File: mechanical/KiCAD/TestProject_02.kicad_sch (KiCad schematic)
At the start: 29 parts, among them J1 USB_C_Receptacle_USB2.0_16P, J2 C-OBD-II-16M, U1 ESP32-C3-WROOM-02, U2 TPS54302, U3 USBLC6-2P6, U4 SN65HVD231

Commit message: Editing the schematic drawing for the OBD PCB, still needs somepolishing and cleaning up.
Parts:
- added D4: SMAJ24A, Diode_SMD:D_SMA, symbol Diode:SMAJ24A
- added D5: LED_G, LED_SMD:LED_0805_2012Metric, symbol Device:LED
- added D6: LED_B, LED_SMD:LED_0805_2012Metric, symbol Device:LED
- added D7: LED_R, LED_SMD:LED_0805_2012Metric, symbol Device:LED
- added D8: SS34, Diode_SMD:D_SMA, symbol Diode:SS34
- added D9: NUP2105L, Package_TO_SOT_SMD:SOT-23, symbol Power_Protection:NUP2105L
- added R11, R12, R13: 330R, Resistor_SMD:R_0603_1608Metric, symbol Device:R
- added R9: 120R, Resistor_SMD:R_0603_1608Metric, symbol Device:R
- D3: value LED -> LED_G
- renumbered RST1 to BTN1
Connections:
- net +3.3V: now also R8.2, U4.3 (VCC), D8.1 (K)
- net GND: now also J2.4, J2.5, U4.2 (GND), D4.2 (A2), D5.1 (K), D6.1 (K), D7.1 (K), D9.3 (A)
- net USB_D+: now also U1.14 (IO19)
- net USB_D-: now also U1.13 (IO18)
- net CAN_TX: now reaches U4.1 (D)
- net CAN_TX: now also U1.4 (IO5)
- net CAN_RX: now reaches U4.4 (R)
- net CAN_RX: now also U1.3 (IO4)
- net CANL: now reaches U4.6 (CANL)
- net CANL: now also J2.14, D9.2 (K), R9.1
- net CANH: now reaches U4.7 (CANH)
- net CANH: now also J2.6, D9.1 (K), R9.2
- net OPMODE: now reaches U4.8 (Rs)
- net OPMODE: now also U1.10 (IO10)
- net at U1.15 (IO3): now also R12.1
- net at U1.17 (IO1): now also R11.1
- net at U1.7 (IO8): now also R13.1
- net at J2.16: now also D4.1 (A1), D8.2 (A)
- new net: D7.2 (A), R13.2
- new net: D5.2 (A), R11.2
- new net: D6.2 (A), R12.2
- no-connect marks 3 -> 15
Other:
- note added: "Connection Indicator LED"
- note added: "Error Indicator LED"
- note added: "Operation mode selector (High speed, standby, low power) Logic is needed for this from the ESP"
- note added: "Over Voltage Protection Diode"
- note added: "Power Indicator LED"
- note added: "TVS Diode ESD, EFT protection"
- moved on the sheet: BTN1, C2, EN1, J2, R1, R7, U4

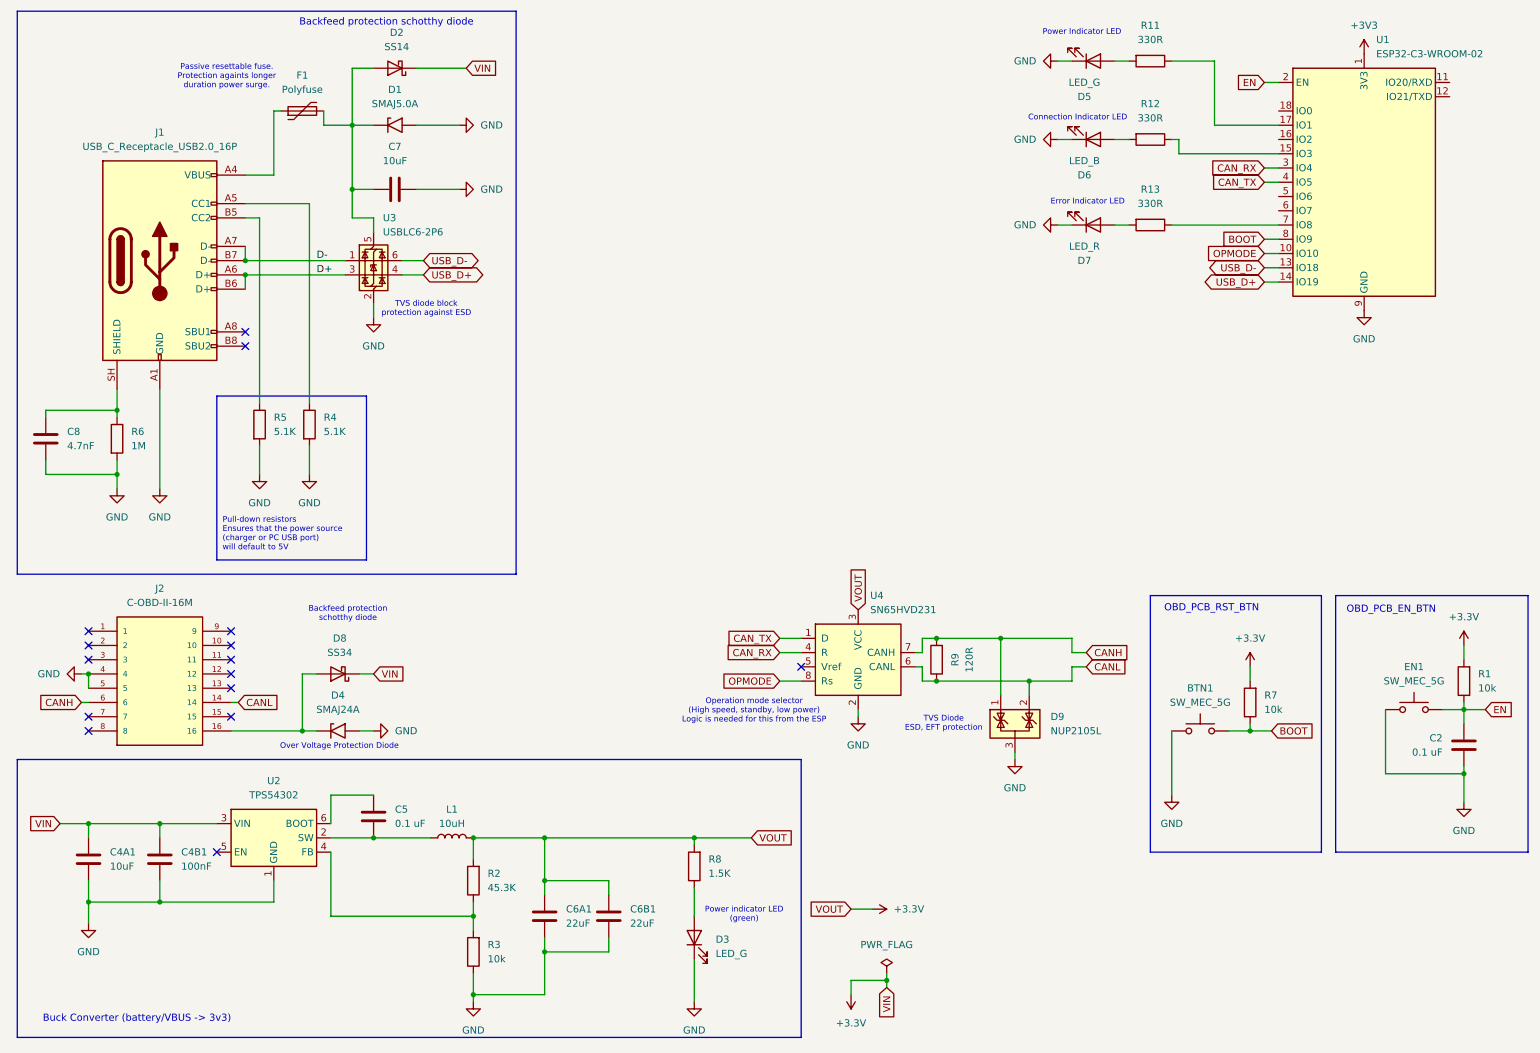
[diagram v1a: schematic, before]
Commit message: Small changes in the schematic layout, organized the components into blocks, changed some wrong footprints
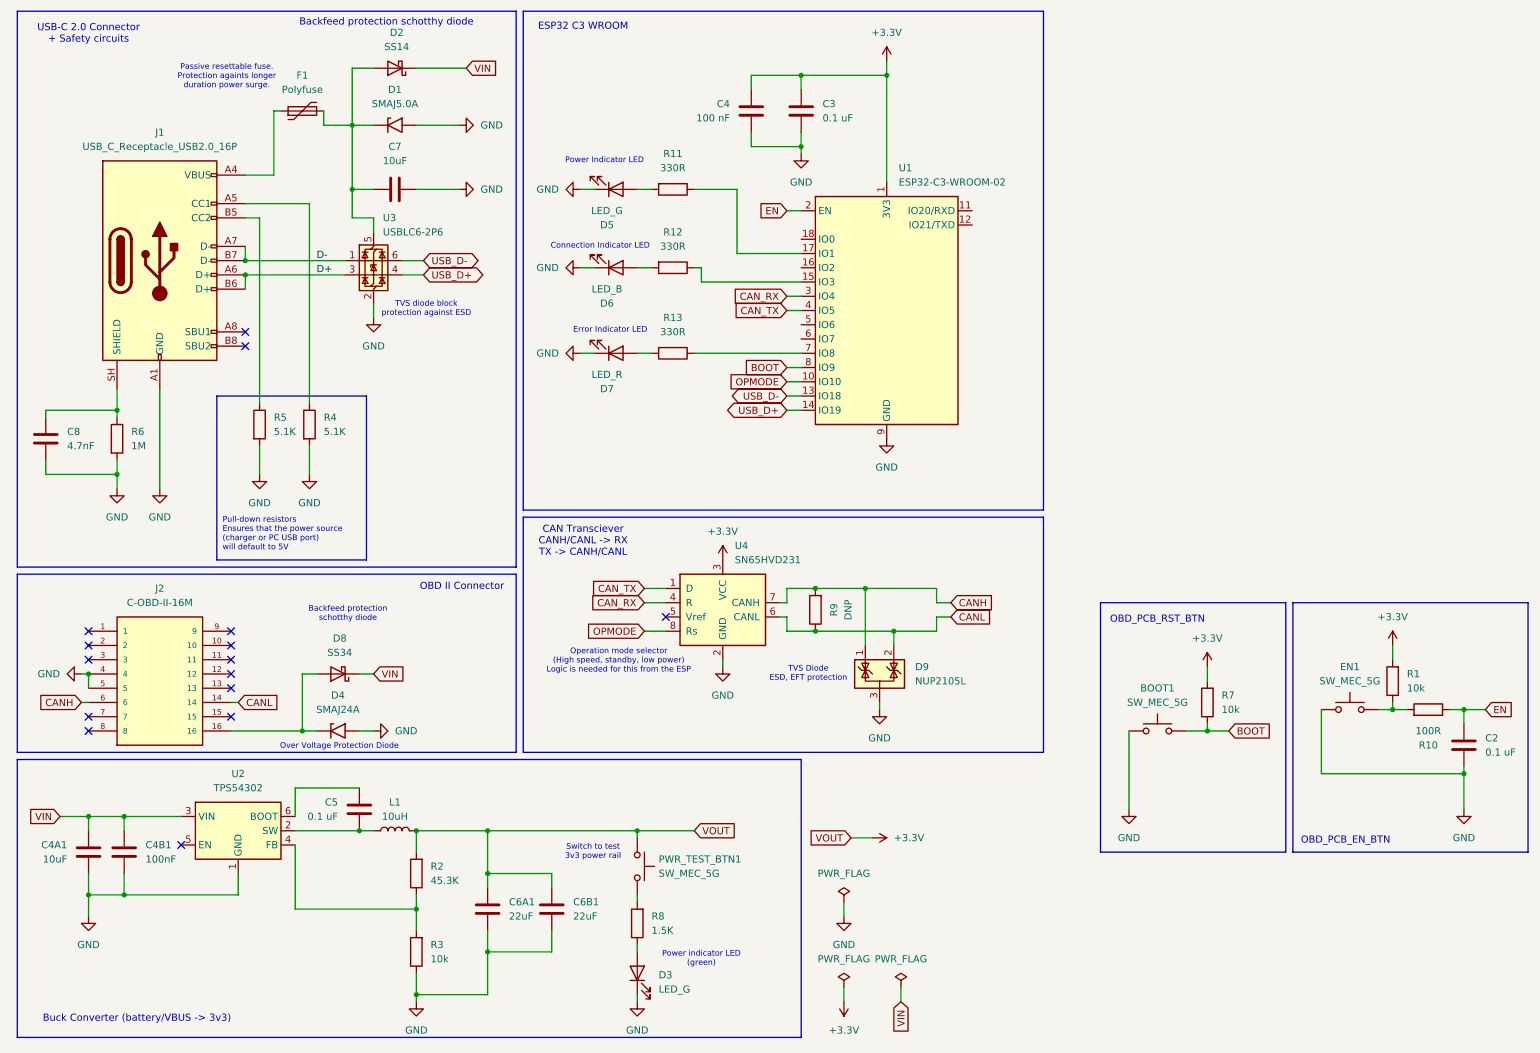
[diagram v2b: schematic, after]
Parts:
- added C3: 0.1 uF, Capacitor_SMD:C_0805_2012Metric, symbol Device:C
- added C4: 100 nF, Capacitor_SMD:C_0805_2012Metric, symbol Device:C
- added PWR_TEST_BTN1: SW_MEC_5G, Button_Switch_SMD:SW_Push_SPST_NO_Alps_SKRK, symbol Switch:SW_MEC_5G
- added R10: 100R, Resistor_SMD:R_0805_2012Metric, symbol Device:R
- BOOT1: renamed from BTN1; footprint Button_Switch_THT:SW_PUSH_1P1T_6x3.5mm_H5.0_APEM_MJTP1250 -> Button_Switch_SMD:SW_Push_SPST_NO_Alps_SKRK
- EN1: footprint Button_Switch_THT:SW_PUSH_1P1T_6x3.5mm_H5.0_APEM_MJTP1250 -> Button_Switch_SMD:SW_Push_SPST_NO_Alps_SKRK
- F1: footprint Fuse:Fuse_Bourns_MF-RHT050 -> Fuse:Fuse_0805_2012Metric
- R11, R12, R13: footprint Resistor_SMD:R_0603_1608Metric -> Resistor_SMD:R_0805_2012Metric
- R9: value 120R -> DNP; footprint Resistor_SMD:R_0603_1608Metric -> Resistor_SMD:R_0805_2012Metric
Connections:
- net +3V3 is gone; now on net +3.3V: U1.1 (3V3)
- net +3.3V: now also C3.1, C4.1, PWR_TEST_BTN1.1 (A), PWR_TEST_BTN1.2 (A); no longer C4A1.1, C4B1.1, D2.1 (K), D8.1 (K), R8.2, U2.3 (VIN)
- net EN: now also R10.1; no longer EN1.3 (B), EN1.4 (B), R1.1
- net GND: now also C3.2, C4.2
- new net: EN1.3 (B), EN1.4 (B), R1.1, R10.2
- new net: PWR_TEST_BTN1.3 (B), PWR_TEST_BTN1.4 (B), R8.2
- new net VIN: C4A1.1, C4B1.1, D2.1 (K), D8.1 (K), U2.3 (VIN)
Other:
- note added: "CAN Transciever CANH/CANL -> RX TX -> CANH/CANL"
- note added: "ESP32 C3 WROOM"
- note added: "OBD II Connector"
- note added: "Switch to test 3v3 power rail"
- note added: "USB-C 2.0 Connector + Safety circuits"
- moved on the sheet: BOOT1, C4A1, C4B1, C5, C6A1, C6B1, D3, D5, D6, D7, D9, EN1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

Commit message: Getting close to finishing the OBD PCB. Still needs some final touch ups, also some safety and reliability check.
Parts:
- removed BOOT1, EN1, PWR_TEST_BTN1: SW_MEC_5G, Button_Switch_SMD:SW_Push_SPST_NO_Alps_SKRK, symbol Switch:SW_MEC_5G
- removed R9: DNP, Resistor_SMD:R_0805_2012Metric, symbol Device:R
- added BOOT2, EN1, TEST_BTN1: SW_MEC_5E, Button_Switch_SMD:SW_SPST_EVQP2_MiddlePushTravel_H2.5mm, symbol Switch:SW_MEC_5E
- added JP1: SolderJumper_2_Open, Jumper:SolderJumper-2_P1.3mm_Open_Pad1.0x1.5mm, symbol Jumper:SolderJumper_2_Open
- C4A1: footprint Capacitor_SMD:C_1206_3216Metric -> Capacitor_SMD:C_0805_2012Metric
- J2: footprint custom_library:COMTECH_C-OBD-II-16M -> C-OBD-II-16M:COMTECH_C-OBD-II-16M
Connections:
- net +3.3V: now also TEST_BTN1.1
- net BOOT: now also BOOT2.1
- net CANH: now also JP1.2 (B)
- net CANL: now also JP1.1 (A)
- net CAN_RX: now also U1.4 (IO5); no longer U1.3 (IO4)
- net CAN_TX: now also U1.3 (IO4); no longer U1.4 (IO5)
- net GND: now also BOOT2.2, EN1.2
- net at R11.1: now also U1.5 (IO6); no longer U1.17 (IO1)
- net at R1.1, R10.2: now also EN1.1
- net at U1.15 (IO3): no longer R12.1
- net at U1.6 (IO7): now also R12.1
- net at R8.2: now also TEST_BTN1.2
- new net: TEST_BTN1.3 (K), TEST_BTN1.4 (A)
- new net: BOOT2.3 (K), BOOT2.4 (A)
- new net: EN1.3 (K), EN1.4 (A)
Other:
- moved on the sheet: D3, D5, D6, D7, R11, R12, R13, R8

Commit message: Relocated buck converter and CAN transciever, added a mounting hole to secure the casing later.
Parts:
- added J3: TXD_PAD, TestPoint:TestPoint_Pad_2.0x2.0mm, symbol Connector:Conn_01x01_Pin
- added J4: RXD_PAD, TestPoint:TestPoint_Pad_2.0x2.0mm, symbol Connector:Conn_01x01_Pin
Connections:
- net at U1.11 (IO20/RXD): now also J3.1 (Pin_1)
- net at U1.12 (IO21/TXD): now also J4.1 (Pin_1)
- no-connect marks 15 -> 19
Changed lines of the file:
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@@
 	(rectangle
 		(start 104.14 13.97)
-		(end 196.85 102.87)
+		(end 210.82 102.87)
 		(stroke
 			(width 0)
@@
 	)
 	(junction
-		(at 170.18 125.73)
-		(diameter 0)
-		(color 0 0 0 0)
-	)
-	(junction
 		(at 97.79 160.02)
 		(diameter 0)
@@
 	)
 	(junction
+		(at 170.18 125.73)
+		(diameter 0)
+		(color 0 0 0 0)
+	)
+	(junction
 		(at 54.61 58.42)
 		(diameter 0)
@@
 	)
 	(no_connect
+		(at 153.67 59.69)
+	)
+	(no_connect
 		(at 54.61 71.12)
 	)
 	(no_connect
+		(at 153.67 62.23)
+	)
+	(no_connect
 		(at 52.07 134.62)
 	)
@@
 	)
 	(no_connect
+		(at 153.67 57.15)
+	)
+	(no_connect
+		(at 153.67 54.61)
+	)
+	(no_connect
 		(at 26.67 142.24)
 	)
@@
 	(wire
 		(pts
+			(xy 165.1 115.57) (xy 177.8 115.57)
+		)
+		(stroke
+			(width 0)
+			(type default)
+		)
+	)
+	(wire
+		(pts
 			(xy 177.8 121.92) (xy 177.8 125.73)
 		)
@@
 	(wire
 		(pts
+			(xy 186.69 54.61) (xy 186.69 52.07)
+		)
+		(stroke
+			(width 0)
+			(type default)
+		)
+	)
+	(wire
+		(pts
 			(xy 26.67 171.45) (xy 26.67 175.26)
 		)
@@
 	(wire
 		(pts
+			(xy 170.18 125.73) (xy 170.18 127)
+		)
+		(stroke
+			(width 0)
+			(type default)
+		)
+	)
+	(wire
+		(pts
 			(xy 97.79 167.64) (xy 97.79 160.02)
 		)
@@
 	(wire
 		(pts
+			(xy 186.69 52.07) (xy 184.15 52.07)
+		)
+		(stroke
+			(width 0)
+			(type default)
+		)
+	)
+	(wire
+		(pts
 			(xy 73.66 34.29) (xy 77.47 34.29)
 		)
@@
 	(wire
 		(pts
-			(xy 68.58 34.29) (xy 73.66 34.29)
+			(xy 170.18 125.73) (xy 177.8 125.73)
 		)
 		(stroke
@@
 	(wire
 		(pts
-			(xy 39.37 81.28) (xy 39.37 99.06)
+			(xy 68.58 34.29) (xy 73.66 34.29)
 		)
 		(stroke
@@
 	(wire
 		(pts
-			(xy 64.77 132.08) (xy 67.31 132.08)
+			(xy 39.37 81.28) (xy 39.37 99.06)
 		)
 		(stroke
@@
 	(wire
 		(pts
-			(xy 177.8 119.38) (xy 177.8 115.57)
+			(xy 64.77 132.08) (xy 67.31 132.08)
 		)
 		(stroke
@@
 	(wire
 		(pts
-			(xy 170.18 125.73) (xy 177.8 125.73)
+			(xy 177.8 119.38) (xy 177.8 115.57)
 		)
 		(stroke
@@
 	(wire
 		(pts
-			(xy 165.1 115.57) (xy 177.8 115.57)
-		)
-		(stroke
-			(width 0)
-			(type default)
-		)
-	)
-	(wire
-		(pts
 			(xy 151.13 77.47) (xy 153.67 77.47)
 		)
@@
 	(wire
 		(pts
+			(xy 165.1 115.57) (xy 165.1 127)
+		)
+		(stroke
+			(width 0)
+			(type default)
+		)
+	)
+	(wire
+		(pts
 			(xy 151.13 121.92) (xy 151.13 125.73)
 		)
@@
 	(wire
 		(pts
-			(xy 168.91 22.86) (xy 168.91 25.4)
+			(xy 184.15 49.53) (xy 189.23 49.53)
 		)
 		(stroke
@@
 	(wire
 		(pts
-			(xy 161.29 187.96) (xy 161.29 190.5)
+			(xy 168.91 22.86) (xy 168.91 25.4)
 		)
 		(stroke
@@
 	(wire
 		(pts
-			(xy 165.1 115.57) (xy 165.1 127)
+			(xy 161.29 187.96) (xy 161.29 190.5)
 		)
 		(stroke
@@
 	(wire
 		(pts
+			(xy 189.23 49.53) (xy 189.23 62.23)
+		)
+		(stroke
+			(width 0)
+			(type default)
+		)
+	)
+	(wire
+		(pts
 			(xy 256.54 138.43) (xy 259.08 138.43)
 		)
@@
 	(wire
 		(pts
-			(xy 170.18 125.73) (xy 170.18 127)
-		)
-		(stroke
-			(width 0)
-			(type default)
-		)
-	)
-	(wire
-		(pts
 			(xy 135.89 170.18) (xy 135.89 172.72)
 		)
@@
 	)
 	(symbol
+		(lib_id "Connector:Conn_01x01_Pin")
+		(at 186.69 59.69 90)
+		(unit 1)
+		(body_style 1)
+		(exclude_from_sim no)
+		(in_bom yes)
+		(on_board yes)
+		(in_pos_files yes)
+		(dnp no)
+		(property "Reference" "J4"
+			(at 189.484 55.88 90)
+			(show_name no)
+			(do_not_autoplace no)
+			(effects
+				(font
+					(size 1.27 1.27)
+				)
+				(justify right)
+			)
+		)
+		(property "Value" "RXD_PAD"
+			(at 189.484 58.42 90)
+			(show_name no)
+			(do_not_autoplace no)
+			(effects
+				(font
+					(size 1.27 1.27)
+				)
+				(justify right)
+			)
+		)
+		(property "Footprint" "TestPoint:TestPoint_Pad_2.0x2.0mm"
+			(at 186.69 59.69 0)
+			(hide yes)
+			(show_name no)
+			(do_not_autoplace no)
+			(effects
+				(font
+					(size 1.27 1.27)
+				)
+			)
+		)
+		(property "Datasheet" ""
+			(at 186.69 59.69 0)
+			(hide yes)
+			(show_name no)
+			(do_not_autoplace no)
+			(effects
+				(font
+					(size 1.27 1.27)
+				)
+			)
+		)
+		(property "Description" "Generic connector, single row, 01x01, script generated"
+			(at 186.69 59.69 0)
+			(hide yes)
+			(show_name no)
+			(do_not_autoplace no)
+			(effects
+				(font
+					(size 1.27 1.27)
+				)
+			)
+		)
+		(pin "1"
+		)
+		(instances
+			(project "TestProject_02"
+				(path "/7255cca5-8951-4933-ab1b-c278e0bd5ab4"
+					(reference "J4")
+					(unit 1)
+				)
+			)
+		)
+	)
+	(symbol
 		(lib_id "Device:R")
 		(at 132.08 58.42 270)
@@
 					(unit 1)
 				)
+			)
+		)
+	)
+	(symbol
+		(lib_id "Connector:Conn_01x01_Pin")
+		(at 189.23 67.31 90)
+		(unit 1)
+		(body_style 1)
+		(exclude_from_sim no)
+		(in_bom yes)
+		(on_board yes)
+		(in_pos_files yes)
+		(dnp no)
+		(property "Reference" "J3"
+			(at 189.992 63.5 90)
+			(show_name no)
+			(do_not_autoplace no)
+			(effects
+				(font
+					(size 1.27 1.27)
+				)
+				(justify right)
+			)
+		)
+		(property "Value" "TXD_PAD"
+			(at 189.992 66.04 90)
+			(show_name no)
+			(do_not_autoplace no)
+			(effects
+				(font
+					(size 1.27 1.27)
+				)
+				(justify right)
+			)
+		)
+		(property "Footprint" "TestPoint:TestPoint_Pad_2.0x2.0mm"
+			(at 189.23 67.31 0)
+			(hide yes)
+			(show_name no)
+			(do_not_autoplace no)
+			(effects
+				(font
+					(size 1.27 1.27)
+				)
+			)
+		)
+		(property "Datasheet" ""
+			(at 189.23 67.31 0)
+			(hide yes)
+			(show_name no)
+			(do_not_autoplace no)
+			(effects
+				(font
+					(size 1.27 1.27)
+				)
+			)
+		)
+		(property "Description" "Generic connector, single row, 01x01, script generated"
+			(at 189.23 67.31 0)
+			(hide yes)
+			(show_name no)
+			(do_not_autoplace no)
+			(effects
+				(font
+					(size 1.27 1.27)
+				)
+			)
+		)
+		(pin "1"
+		)
+		(instances
+			(project "TestProject_02"
+				(path "/7255cca5-8951-4933-ab1b-c278e0bd5ab4"
+					(reference "J3")
+					(unit 1)
+				)
